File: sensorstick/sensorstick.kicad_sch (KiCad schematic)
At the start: 24 parts, among them J1 USB-A Header, U1 ESP32-C3_SUPERMINI, U2 SGP30, U3 SHT4x, U4 SCD40-D-R2, U5 PCA9306DC, U6 LP5907MFX-1.8

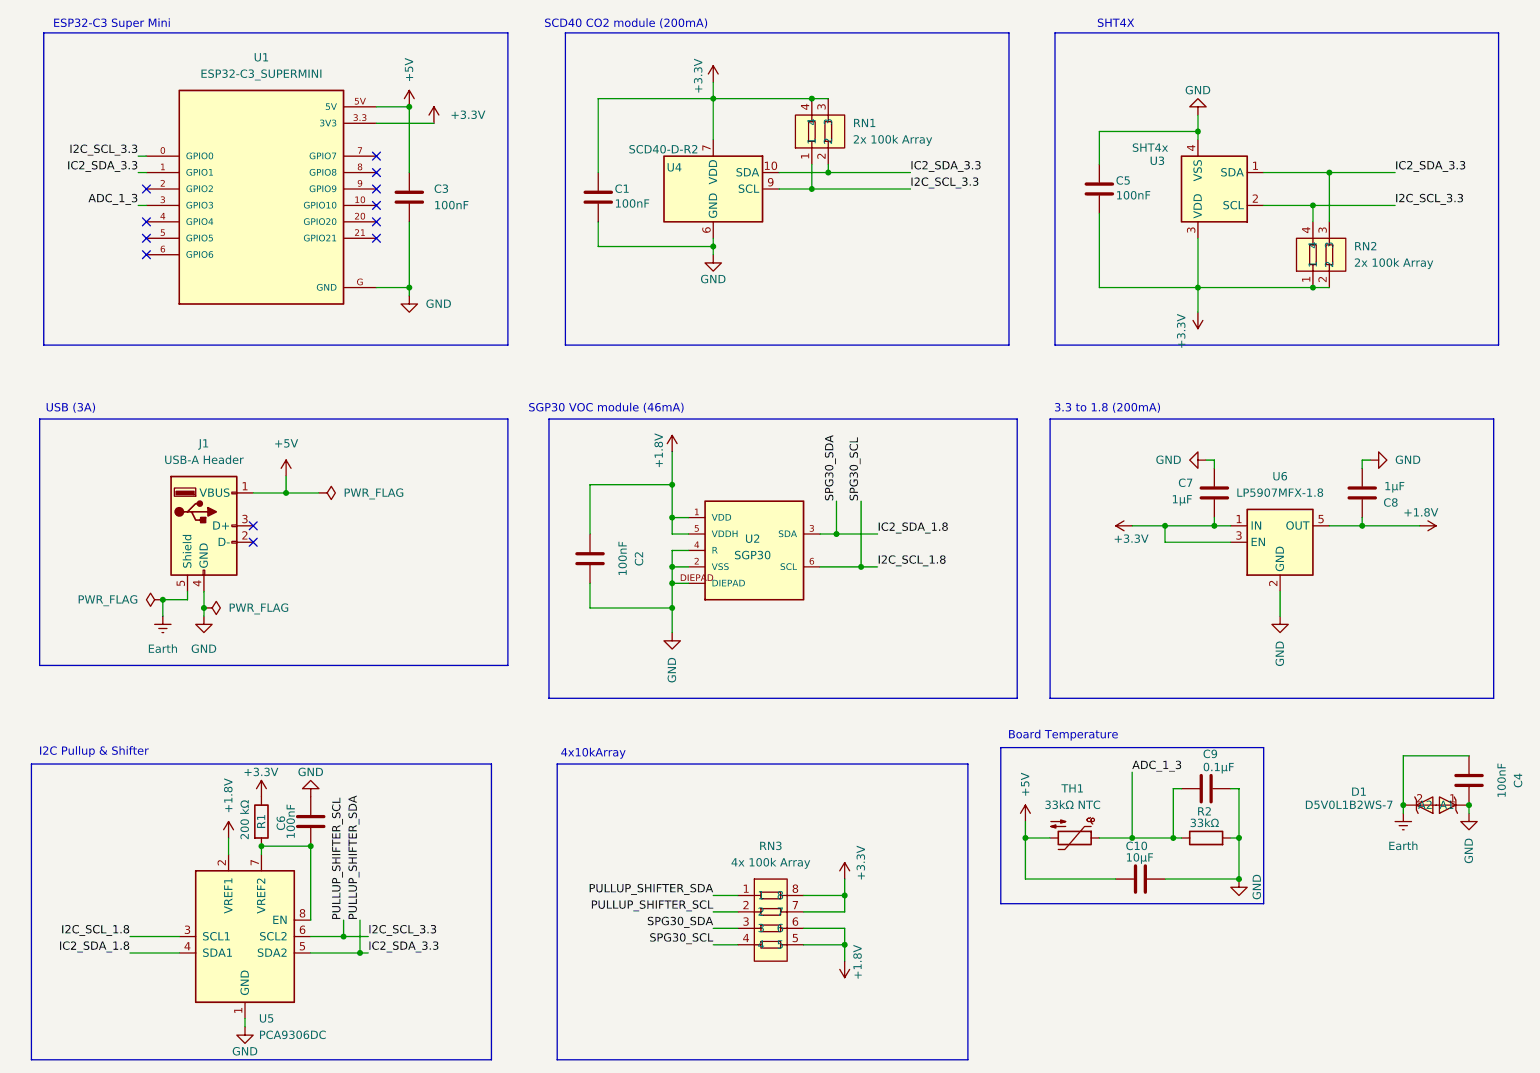
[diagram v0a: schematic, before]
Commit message: changed sgp30 to sgp
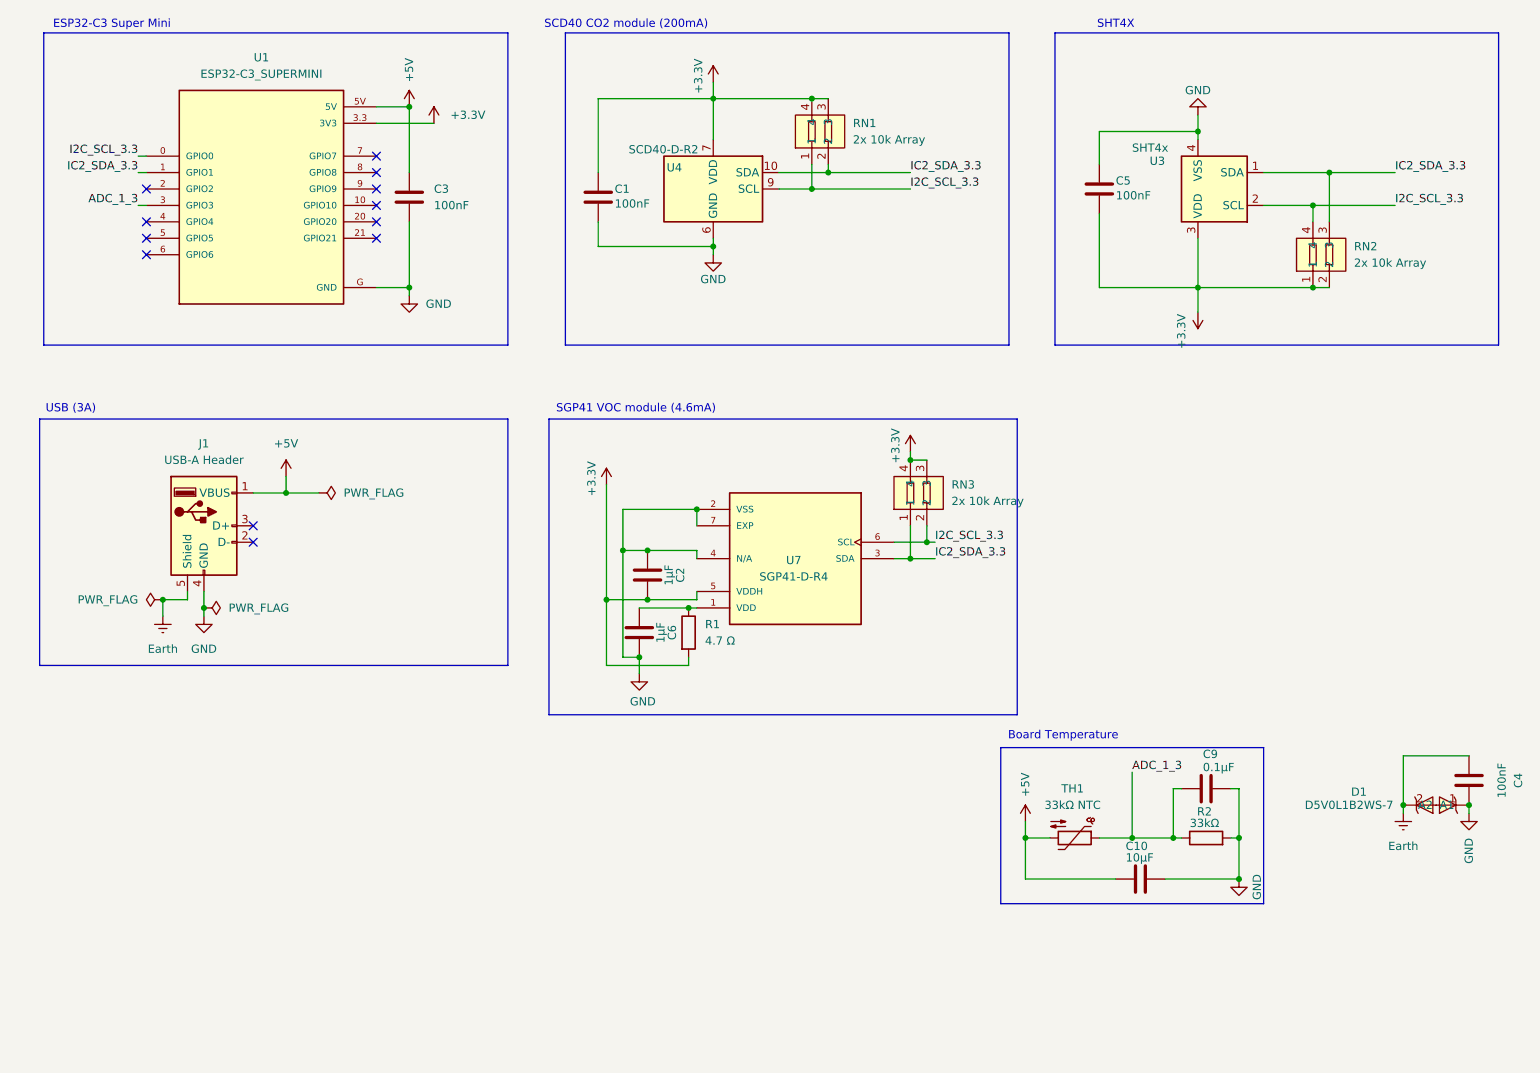
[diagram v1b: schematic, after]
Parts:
- removed C7, C8: 1µF, Capacitor_SMD:C_0603_1608Metric, symbol Device:C
- removed RN3: 4x 100k Array, easyeda2kicad:RES-ARRAY-SMD_0402-8P-L2.0-W1.0-BL, symbol easyeda2kicad:4D02WGF1002TCE
- removed U2: SGP30, SGP30:SGP30, symbol SGP30:SGP30
- removed U5: PCA9306DC, Package_SO:VSSOP-8_2.3x2mm_P0.5mm, symbol Interface:PCA9306DC
- removed U6: LP5907MFX-1.8, Package_TO_SOT_SMD:SOT-23-5, symbol Regulator_Linear:LP5907MFX-1.8
- added RN3: 2x 10k Array, easyeda2kicad:RES-ARRAY-SMD_0402-4P-L1.0-W1.0-BL, symbol easyeda2kicad:2D02WGJ0103TCE
- added U7: SGP41-D-R4, SGP41_D_R4:XDCR_SGP41-D-R4, symbol SGP41:SGP41-D-R4
- C2, C6: value 100nF -> 1μF
- R1: value 200 kΩ -> 4.7 Ω
- RN1, RN2: value 2x 100k Array -> 2x 10k Array
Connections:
- net +1.8V is gone; now on net GND: C2.1
- net +3.3V: now also C2.2, R1.2, RN3.3, RN3.4, U7.5 (VDDH); no longer R1.1
- net GND: now also U7.2 (VSS), U7.4 (N/A), U7.7 (EXP); no longer C2.2
- net I2C_SCL_3.3: now also RN3.2, U7.6 (SCL)
- net IC2_SDA_3.3: now also RN3.1, U7.3 (SDA)
- net at C6.1: now also R1.1, U7.1 (VDD); no longer R1.2
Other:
- note added: "SGP41 VOC module (4.6mA)"
- note removed: "3.3 to 1.8 (200mA)"
- note removed: "4x10kArray"
- note removed: "I2C Pullup & Shifter"
- note removed: "SGP30 VOC module (46mA)"
- moved on the sheet: C2

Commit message: added VEML7700
because of moving from SGP30 to SGP41 I got rid of everything handling 1.8V and 1.8V I²C with space on the pcb I now filled with a High Accuracy Ambient Light Sensor
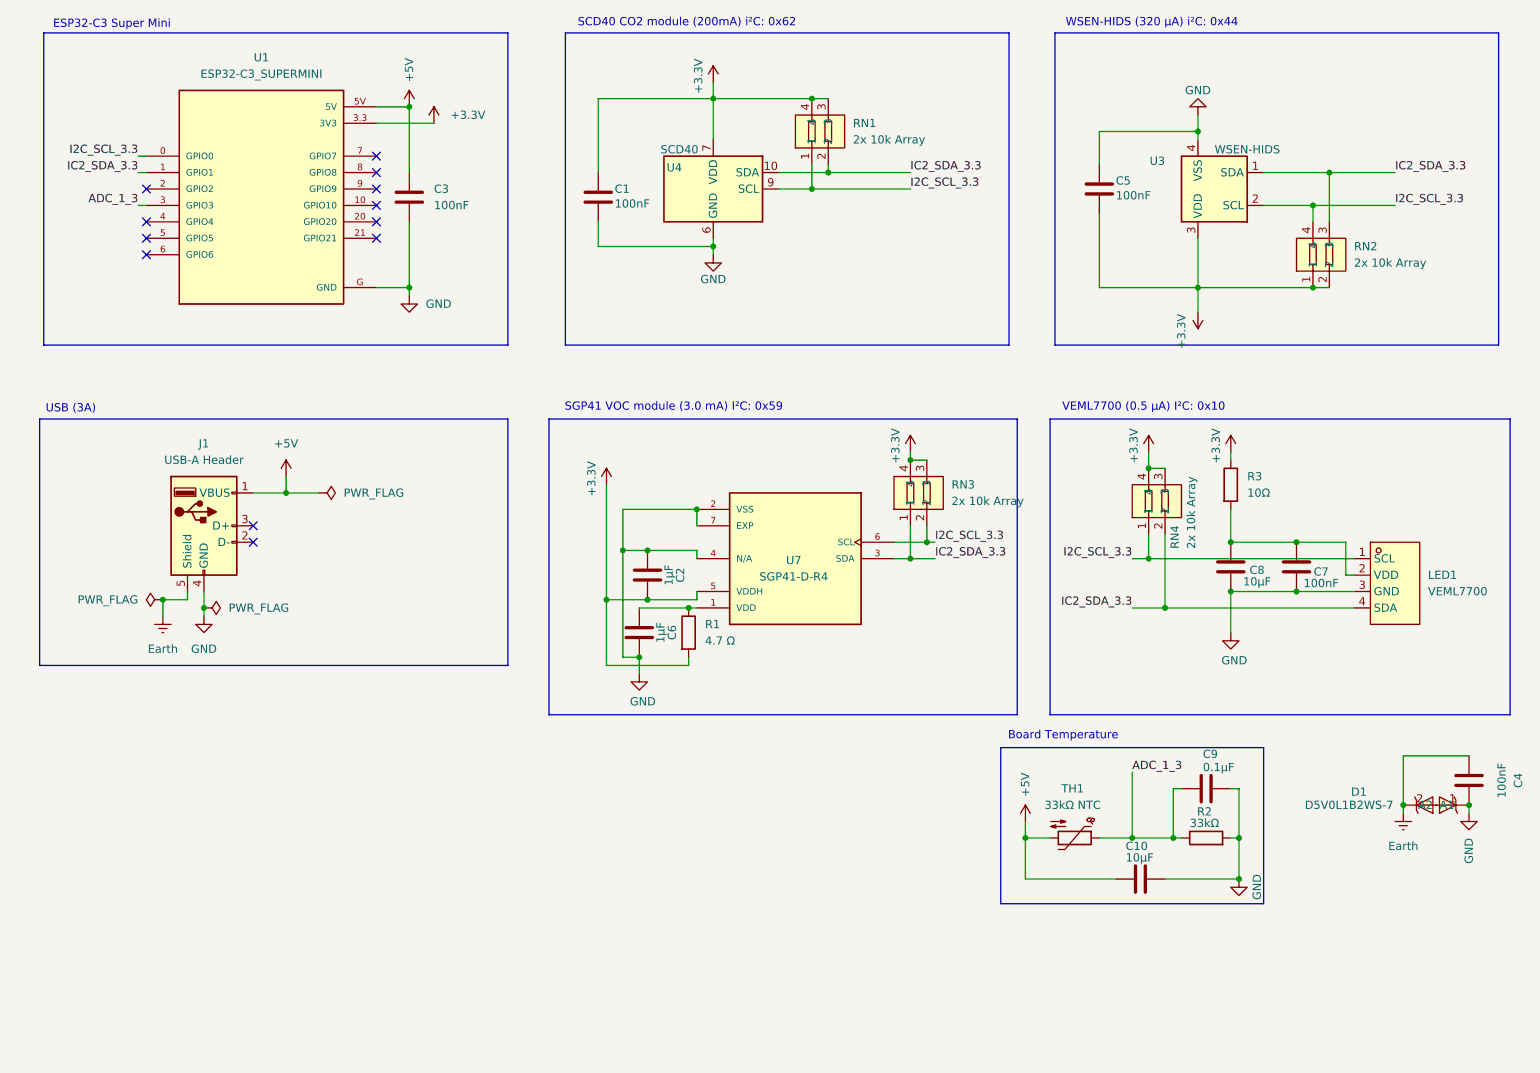
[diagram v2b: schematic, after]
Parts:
- added C7: 100nF, Capacitor_SMD:C_0603_1608Metric, symbol Device:C
- added C8: 10μF, Capacitor_SMD:C_0603_1608Metric, symbol Device:C
- added LED1: VEML7700, easyeda2kicad:LED-SMD_4P-L6.8-W2.4_VEML7700-TR, symbol easyeda2kicad:VEML7700-TR
- added R3: 10Ω, Resistor_SMD:R_0603_1608Metric, symbol Device:R
- added RN4: 2x 10k Array, easyeda2kicad:RES-ARRAY-SMD_0402-4P-L1.0-W1.0-BL, symbol easyeda2kicad:2D02WGJ0103TCE
- U3: value SHT4x -> WSEN-HIDS
- U4: value SCD40-D-R2 -> SCD40
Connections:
- net +3.3V: now also R3.1, RN4.3, RN4.4
- net GND: now also C7.2, C8.2, LED1.3 (GND)
- net I2C_SCL_3.3: now also LED1.1 (SCL), RN4.1
- net IC2_SDA_3.3: now also LED1.4 (SDA), RN4.2
- new net: C7.1, C8.1, LED1.2 (VDD), R3.2
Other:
- note added: "SCD40 CO2 module (200mA) i²C: 0x62"
- note added: "SGP41 VOC module (3.0 mA) I²C: 0x59"
- note added: "VEML7700 (0.5 μA) I²C: 0x10"
- note added: "WSEN-HIDS (320 μA) i²C: 0x44"
- note removed: "SCD40 CO2 module (200mA)"
- note removed: "SGP41 VOC module (4.6mA)"
- note removed: "SHT4X"

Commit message: final touch for ordeing it
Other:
- note added: "SCD40 CO2 module (15mA) i²C: 0x62"
- note removed: "SCD40 CO2 module (200mA) i²C: 0x62"
- moved on the sheet: C2
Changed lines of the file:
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@@
 		)
 	)
-	(text "SCD40 CO2 module (200mA) i²C: 0x62"
+	(text "SCD40 CO2 module (15mA) i²C: 0x62"
 		(exclude_from_sim no)
 		(at 129.286 27.686 0)
@@
 	)
 	(junction
-		(at 123.19 109.22)
-		(diameter 0)
-		(color 0 0 0 0)
-	)
-	(junction
 		(at 240.03 148.59)
 		(diameter 0)
@@
 	)
 	(junction
-		(at 123.19 116.84)
-		(diameter 0)
-		(color 0 0 0 0)
-	)
-	(junction
 		(at 213.36 115.57)
 		(diameter 0)
@@
 	)
 	(junction
+		(at 121.92 116.84)
+		(diameter 0)
+		(color 0 0 0 0)
+	)
+	(junction
 		(at 226.06 55.88)
+		(diameter 0)
+		(color 0 0 0 0)
+	)
+	(junction
+		(at 121.92 109.22)
 		(diameter 0)
 		(color 0 0 0 0)
@@
 	(wire
 		(pts
-			(xy 123.19 116.84) (xy 130.81 116.84)
-		)
-		(stroke
-			(width 0)
-			(type default)
-		)
-	)
-	(wire
-		(pts
 			(xy 161.29 110.49) (xy 163.83 110.49)
 		)
@@
 	(wire
 		(pts
+			(xy 121.92 109.22) (xy 130.81 109.22)
+		)
+		(stroke
+			(width 0)
+			(type default)
+		)
+	)
+	(wire
+		(pts
 			(xy 54.61 115.57) (xy 54.61 118.11)
 		)
@@
 	(wire
 		(pts
-			(xy 123.19 109.22) (xy 130.81 109.22)
-		)
-		(stroke
-			(width 0)
-			(type default)
-		)
-	)
-	(wire
-		(pts
 			(xy 226.06 68.58) (xy 228.6 68.58)
 		)
@@
 	(wire
 		(pts
+			(xy 121.92 116.84) (xy 130.81 116.84)
+		)
+		(stroke
+			(width 0)
+			(type default)
+		)
+	)
+	(wire
+		(pts
 			(xy 218.44 55.88) (xy 226.06 55.88)
 		)
@@
 	(wire
 		(pts
-			(xy 116.84 116.84) (xy 123.19 116.84)
+			(xy 116.84 116.84) (xy 121.92 116.84)
 		)
 		(stroke
@@
 	(wire
 		(pts
-			(xy 119.38 109.22) (xy 123.19 109.22)
+			(xy 119.38 109.22) (xy 121.92 109.22)
 		)
 		(stroke
@@
 	(symbol
 		(lib_id "Device:C")
-		(at 123.19 113.03 0)
+		(at 121.92 113.03 0)
 		(unit 1)
 		(exclude_from_sim no)
@@
 		(dnp no)
 		(property "Reference" "C2"
-			(at 128.27 113.03 90)
+			(at 127 113.03 90)
 			(effects
 				(font
@@
 		)
 		(property "Value" "1μF"
-			(at 126.492 113.03 90)
+			(at 125.222 113.03 90)
 			(effects
 				(font
@@
 		)
 		(property "Footprint" "Capacitor_SMD:C_0603_1608Metric"
-			(at 124.1552 116.84 0)
+			(at 122.8852 116.84 0)
 			(effects
 				(font
@@
 		)
 		(property "Datasheet" "~"
-			(at 123.19 113.03 0)
+			(at 121.92 113.03 0)
 			(effects
 				(font
@@
 		)
 		(property "Description" "Unpolarized capacitor"
-			(at 123.19 113.03 0)
+			(at 121.92 113.03 0)
 			(effects
 				(font
@@
 		)
 		(property "LCSC" "C1591"
-			(at 130.81 113.03 0)
-			(effects
-				(font
+			(at 129.54 113.03 0)
+			(effects
+				(font

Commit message: added partdb id to ci
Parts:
- J1: partdb_id (none) -> 248

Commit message: added partdb ids
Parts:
- C1, C3, C4, C5, C7: partdb_id (none) -> 573
- C10: value 10µF -> 10μF; partdb_id (none) -> 19
- C2, C6: partdb_id (none) -> 428
- C8: partdb_id (none) -> 19
- C9: value 0.1µF -> 100nF; partdb_id (none) -> 573
- D1: partdb_id (none) -> 429
- LED1: partdb_id (none) -> 589
- R1: partdb_id (none) -> 330
- R2: partdb_id (none) -> 559
- R3: partdb_id (none) -> 208
- RN1, RN2, RN3, RN4: partdb_id (none) -> 431
- TH1: partdb_id (none) -> 571
- U1: partdb_id (none) -> 247
- U3: partdb_id (none) -> 584
- U4: partdb_id (none) -> 566
- U7: partdb_id (none) -> 551
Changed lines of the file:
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@@
 			)
 		)
+		(property "partdb_id" "208"
+			(at 213.36 99.06 0)
+			(effects
+				(font
+					(size 1.27 1.27)
+				)
+				(hide yes)
+			)
+		)
 		(pin "1"
 		)
@@
 			)
 		)
-		(property "Value" "10µF"
+		(property "Value" "10μF"
 			(at 197.104 156.718 90)
 			(effects
@@
 			)
 		)
+		(property "partdb_id" "19"
+			(at 199.39 160.02 90)
+			(effects
+				(font
+					(size 1.27 1.27)
+				)
+				(hide yes)
+			)
+		)
 		(pin "2"
 		)
@@
 			)
 		)
+		(property "partdb_id" "429"
+			(at 245.11 148.59 0)
+			(effects
+				(font
+					(size 1.27 1.27)
+				)
+				(hide yes)
+			)
+		)
 		(pin "2"
 		)
@@
 			)
 		)
+		(property "partdb_id" "573"
+			(at 115.57 54.61 0)
+			(effects
+				(font
+					(size 1.27 1.27)
+				)
+				(hide yes)
+			)
+		)
 		(pin "1"
 		)
@@
 			)
 		)
+		(property "partdb_id" "431"
+			(at 201.93 101.6 0)
+			(effects
+				(font
+					(size 1.27 1.27)
+				)
+				(hide yes)
+			)
+		)
 		(pin "4"
 		)
@@
 			)
 		)
+		(property "partdb_id" "431"
+			(at 165.1 100.33 90)
+			(effects
+				(font
+					(size 1.27 1.27)
+				)
+				(hide yes)
+			)
+		)
 		(pin "4"
 		)
@@
 			)
 		)
+		(property "partdb_id" "573"
+			(at 223.52 111.76 0)
+			(effects
+				(font
+					(size 1.27 1.27)
+				)
+				(hide yes)
+			)
+		)
 		(pin "1"
 		)
@@
 			)
 		)
+		(property "partdb_id" "330"
+			(at 129.54 121.92 0)
+			(effects
+				(font
+					(size 1.27 1.27)
+				)
+				(hide yes)
+			)
+		)
 		(pin "1"
 		)
@@
 			)
 		)
+		(property "partdb_id" "431"
+			(at 227.33 63.5 90)
+			(effects
+				(font
+					(size 1.27 1.27)
+				)
+				(hide yes)
+			)
+		)
 		(pin "4"
 		)
@@
 			)
 		)
+		(property "partdb_id" "571"
+			(at 189.23 153.67 90)
+			(effects
+				(font
+					(size 1.27 1.27)
+				)
+				(hide yes)
+			)
+		)
 		(pin "1"
 		)
@@
 			)
 		)
+		(property "partdb_id" "428"
+			(at 121.92 113.03 90)
+			(effects
+				(font
+					(size 1.27 1.27)
+				)
+				(hide yes)
+			)
+		)
 		(pin "1"
 		)
@@
 			)
 		)
+		(property "partdb_id" "573"
+			(at 250.19 144.78 90)
+			(effects
+				(font
+					(size 1.27 1.27)
+				)
+				(hide yes)
+			)
+		)
 		(pin "1"
 		)
@@
 			)
 		)
+		(property "partdb_id" "573"
+			(at 193.04 53.34 0)
+			(effects
+				(font
+					(size 1.27 1.27)
+				)
+				(hide yes)
+			)
+		)
 		(pin "1"
 		)
@@
 			)
 		)
+		(property "partdb_id" "247"
+			(at 63.5 53.34 0)
+			(effects
+				(font
+					(size 1.27 1.27)
+				)
+				(hide yes)
+			)
+		)
 		(pin "21"
 		)
@@
 			)
 		)
-		(property "Value" "0.1µF"
+		(property "Value" "100nF"
 			(at 209.042 142.748 90)
 			(effects
@@
 			)
 		)
+		(property "partdb_id" "573"
+			(at 209.55 146.05 90)
+			(effects
+				(font
+					(size 1.27 1.27)
+				)
+				(hide yes)
+			)
+		)
 		(pin "2"
 		)
@@
 			)
 		)
+		(property "partdb_id" "19"
+			(at 213.36 111.76 0)
+			(effects
+				(font
+					(size 1.27 1.27)
+				)
+				(hide yes)
+			)
+		)
 		(pin "1"
 		)
@@
 			)
 		)
+		(property "partdb_id" "573"
+			(at 86.36 54.61 0)
+			(effects
+				(font
+					(size 1.27 1.27)
+				)
+				(hide yes)
+			)
+		)
 		(pin "1"
 		)
@@
 			)
 		)
+		(property "partdb_id" "589"
+			(at 238.76 114.3 0)
+			(effects
+				(font
+					(size 1.27 1.27)
+				)
+				(hide yes)
+			)
+		)
 		(pin "1"
 		)
@@
 			)
 		)
+		(property "partdb_id" "431"
+			(at 149.86 44.45 90)
+			(effects
+				(font
+					(size 1.27 1.27)
+				)
+				(hide yes)
+			)
+		)
 		(pin "4"
 		)
@@
 			)
 		)
+		(property "partdb_id" "551"
+			(at 146.05 110.49 0)
+			(effects
+				(font
+					(size 1.27 1.27)
+				)
+				(hide yes)
+			)
+		)
 		(pin "7"
 		)
@@
 			)
 		)
+		(property "partdb_id" "566"
+			(at 133.35 53.34 0)
+			(effects
+				(font
+					(size 1.27 1.27)
+				)
+				(hide yes)
+			)
+		)
 		(pin "19"
 		)
@@
 			)
 		)
+		(property "partdb_id" "584"
+			(at 210.82 53.34 0)
+			(effects
+				(font
+					(size 1.27 1.27)
+				)
+				(hide yes)
+			)
+		)
 		(pin "4"
 		)
@@
 			)
 		)
+		(property "partdb_id" "428"
+			(at 121.92 121.92 90)
+			(effects
+				(font
+					(size 1.27 1.27)
+				)
+				(hide yes)
+			)
+		)
 		(pin "1"
 		)
@@
 			)
 		)
+		(property "partdb_id" "559"
+			(at 209.55 153.67 90)
+			(effects
+				(font
+					(size 1.27 1.27)
+				)
+				(hide yes)
+			)
+		)
